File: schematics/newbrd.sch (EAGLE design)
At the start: 37 parts, among them IC1 TLC271D, IC2 TLC271D

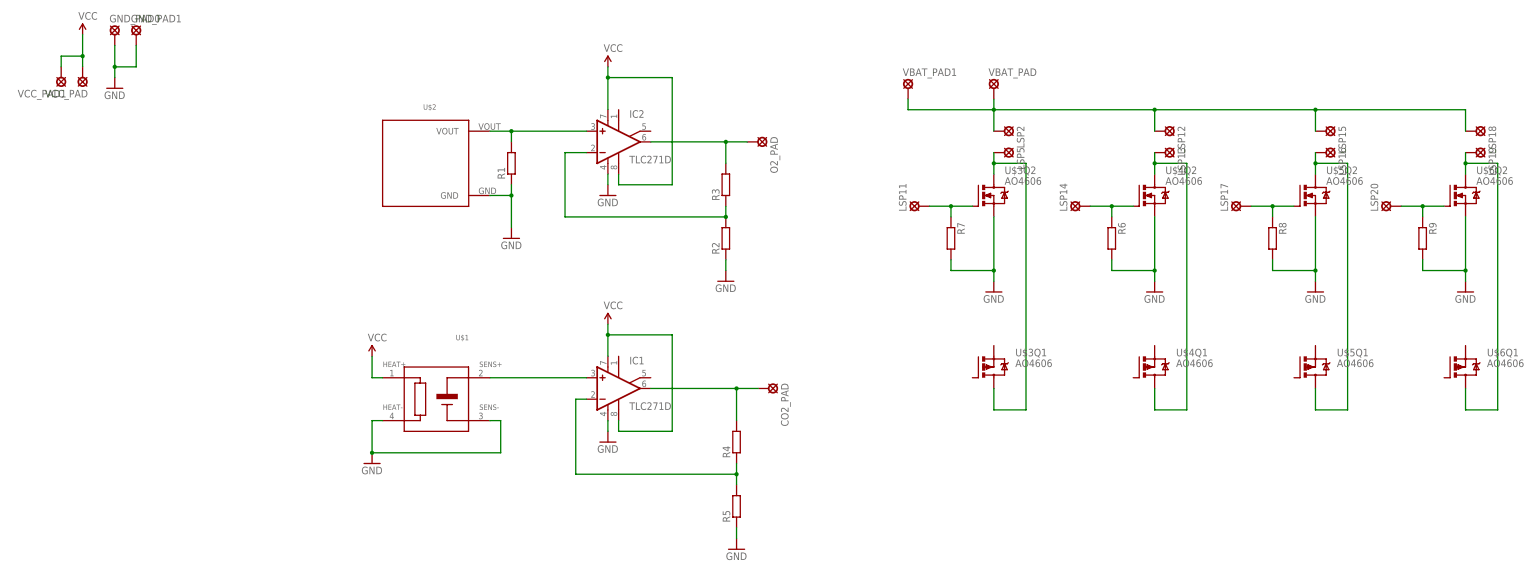
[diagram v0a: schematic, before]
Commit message: Правки платы для аналоговых устройств и доделана плата для I2C устройств
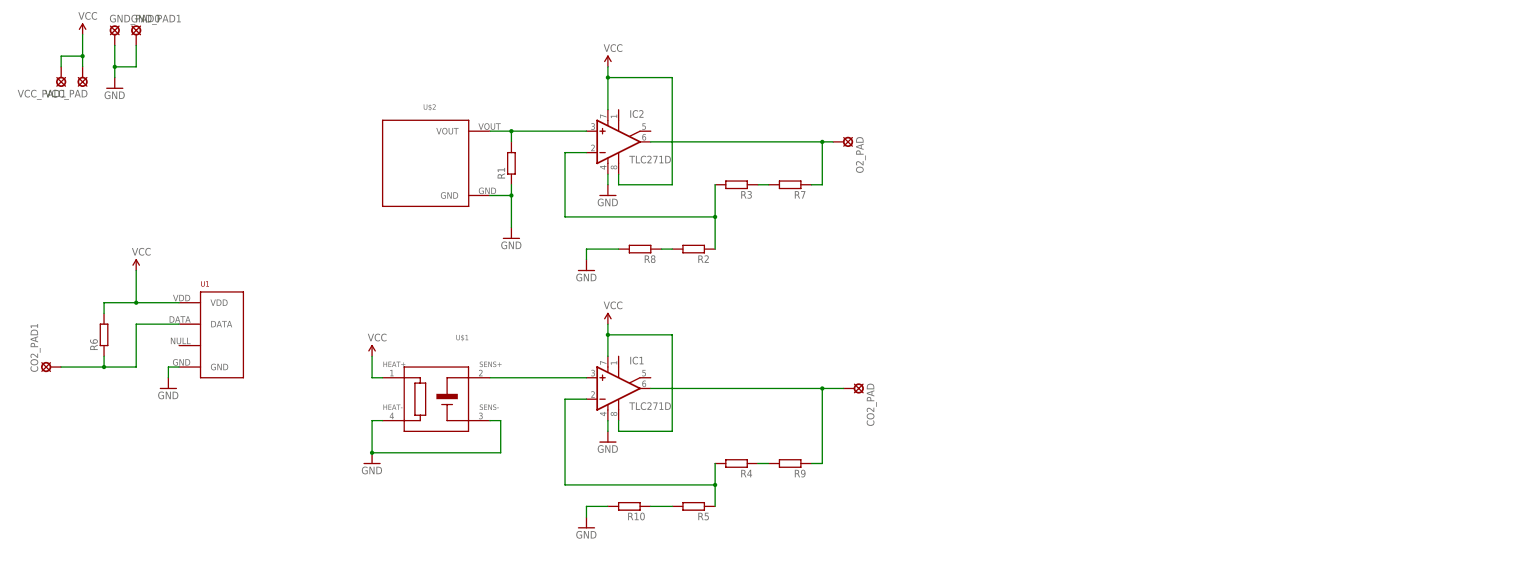
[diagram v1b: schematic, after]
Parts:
- removed LSP11, LSP12, LSP13, LSP14, LSP15, LSP16, LSP17, LSP18, LSP19, LSP2, LSP20, LSP5, VBAT_PAD, VBAT_PAD1: LSP10, solpad:LSP10
- removed U$3, U$4, U$5, U$6: AO4606, elements:AO4606
- added CO2_PAD1: LSP10, solpad:LSP10
- added R10: (no value), resistor:R-EU_R0805
- added U1: (no value), RHT03_DHT-22_AM2302:RHT03_DHT-22_AM2302RA
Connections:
- removed net N$12: LSP13.MP, U$4Q1.D, U$4Q2.D
- removed net N$15: LSP16.MP, U$5Q1.D, U$5Q2.D
- removed net N$16: LSP17.MP, R8.1, U$5Q2.G
- removed net N$18: LSP19.MP, U$6Q1.D, U$6Q2.D
- removed net N$19: LSP20.MP, R9.1, U$6Q2.G
- removed net N$9: IC1.-IN, R4.1, R5.2
- new net N$11: R10.1, R5.2
- new net N$2: CO2_PAD1.MP, R6.1, U1.DATA
- net GND: now also R10.2, U1.GND; no longer R2.1, R5.1, R6.2, R7.2, R9.2, U$3Q2.S, U$4Q2.S, U$5Q2.S, U$6Q2.S
- net N$10: now also R4.1, R9.2; no longer LSP11.MP, R7.1, U$3Q2.G
- net N$13: now also IC1.-IN, R4.2, R5.1; no longer LSP14.MP, R6.1, U$4Q2.G
- net N$3: now also R2.1, R3.2; no longer R2.2, R3.1
- net N$4: now also R7.1; no longer R3.2
- net N$6: now also R9.1; no longer R4.2
- net N$7: now also R3.1, R7.2; no longer LSP12.MP, LSP15.MP, LSP18.MP, LSP2.MP, VBAT_PAD.MP, VBAT_PAD1.MP
- net N$8: now also R2.2, R8.1; no longer LSP5.MP, U$3Q1.D, U$3Q2.D
- net VCC: now also R6.2, U1.VDD
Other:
- moved on the sheet: CO2_PAD, O2_PAD, R2, R3, R4, R5, R6, R7, R8, R9
